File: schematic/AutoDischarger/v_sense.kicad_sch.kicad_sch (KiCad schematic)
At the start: 37 parts, among them IC3 TLV9102SIDGSR, IC4 TLV9102SIDGSR, IC5 TLV9102SIDGSR

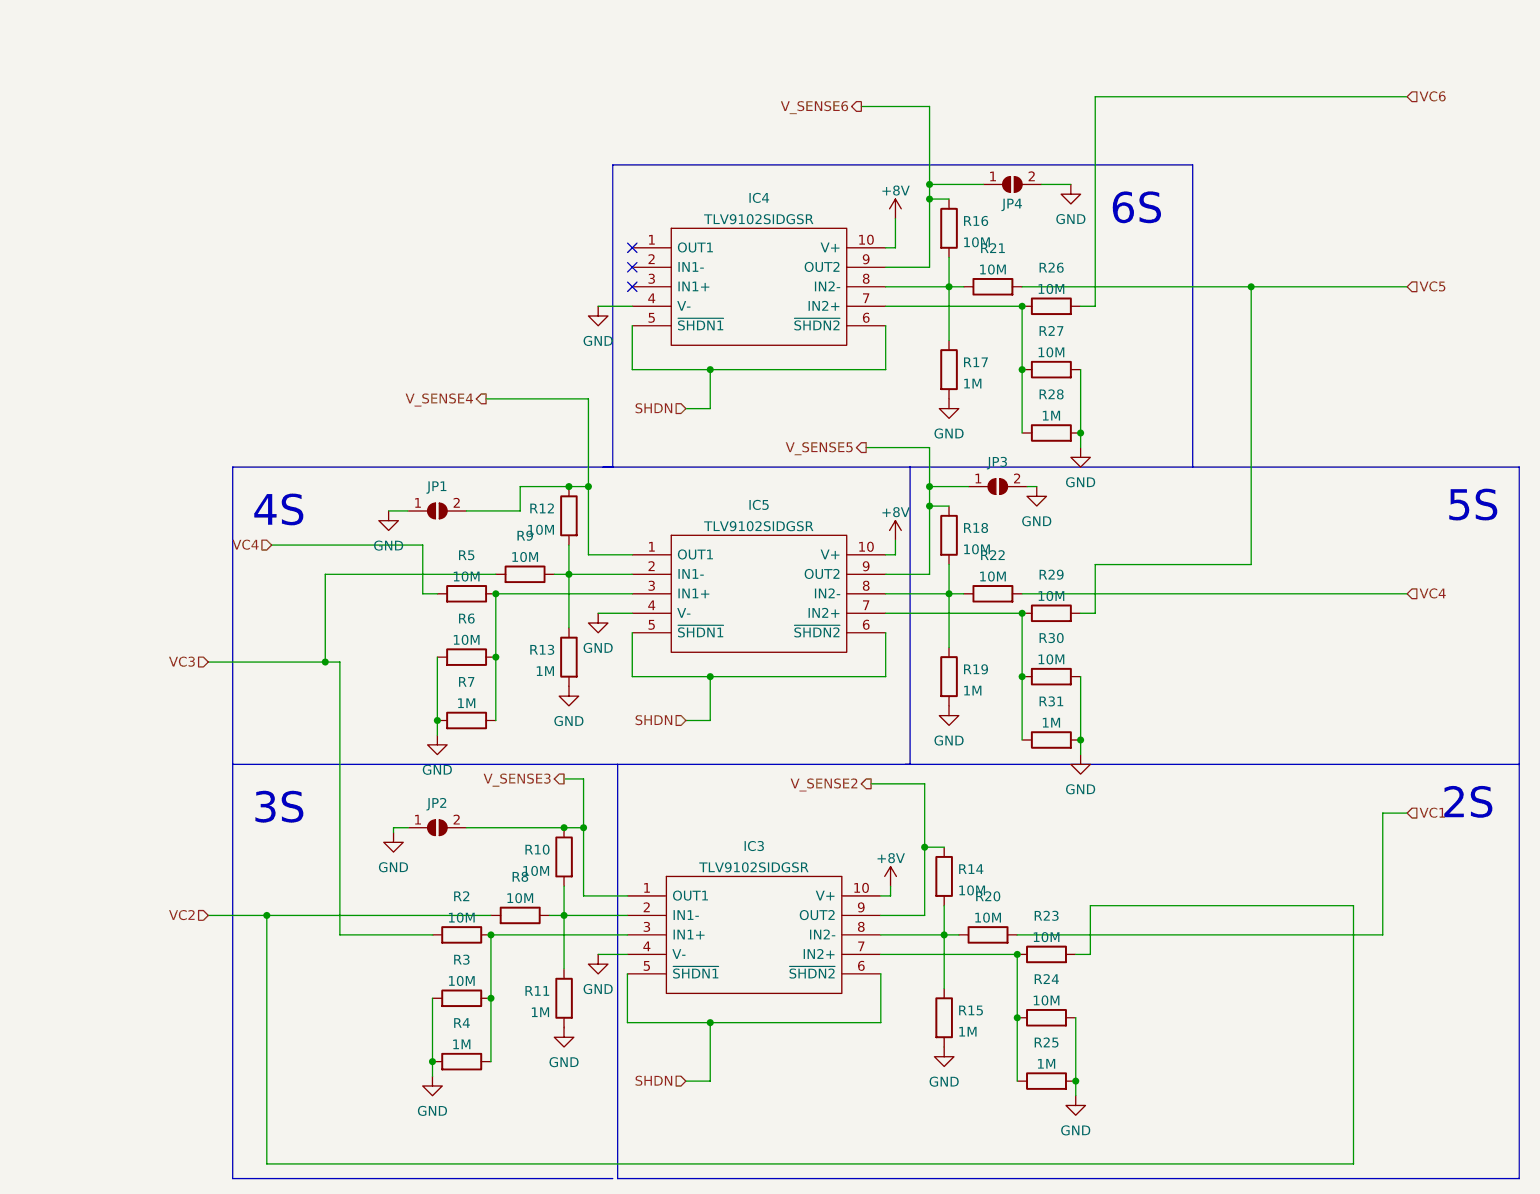
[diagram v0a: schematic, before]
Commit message: Some schematic fixes and assigned footprints.
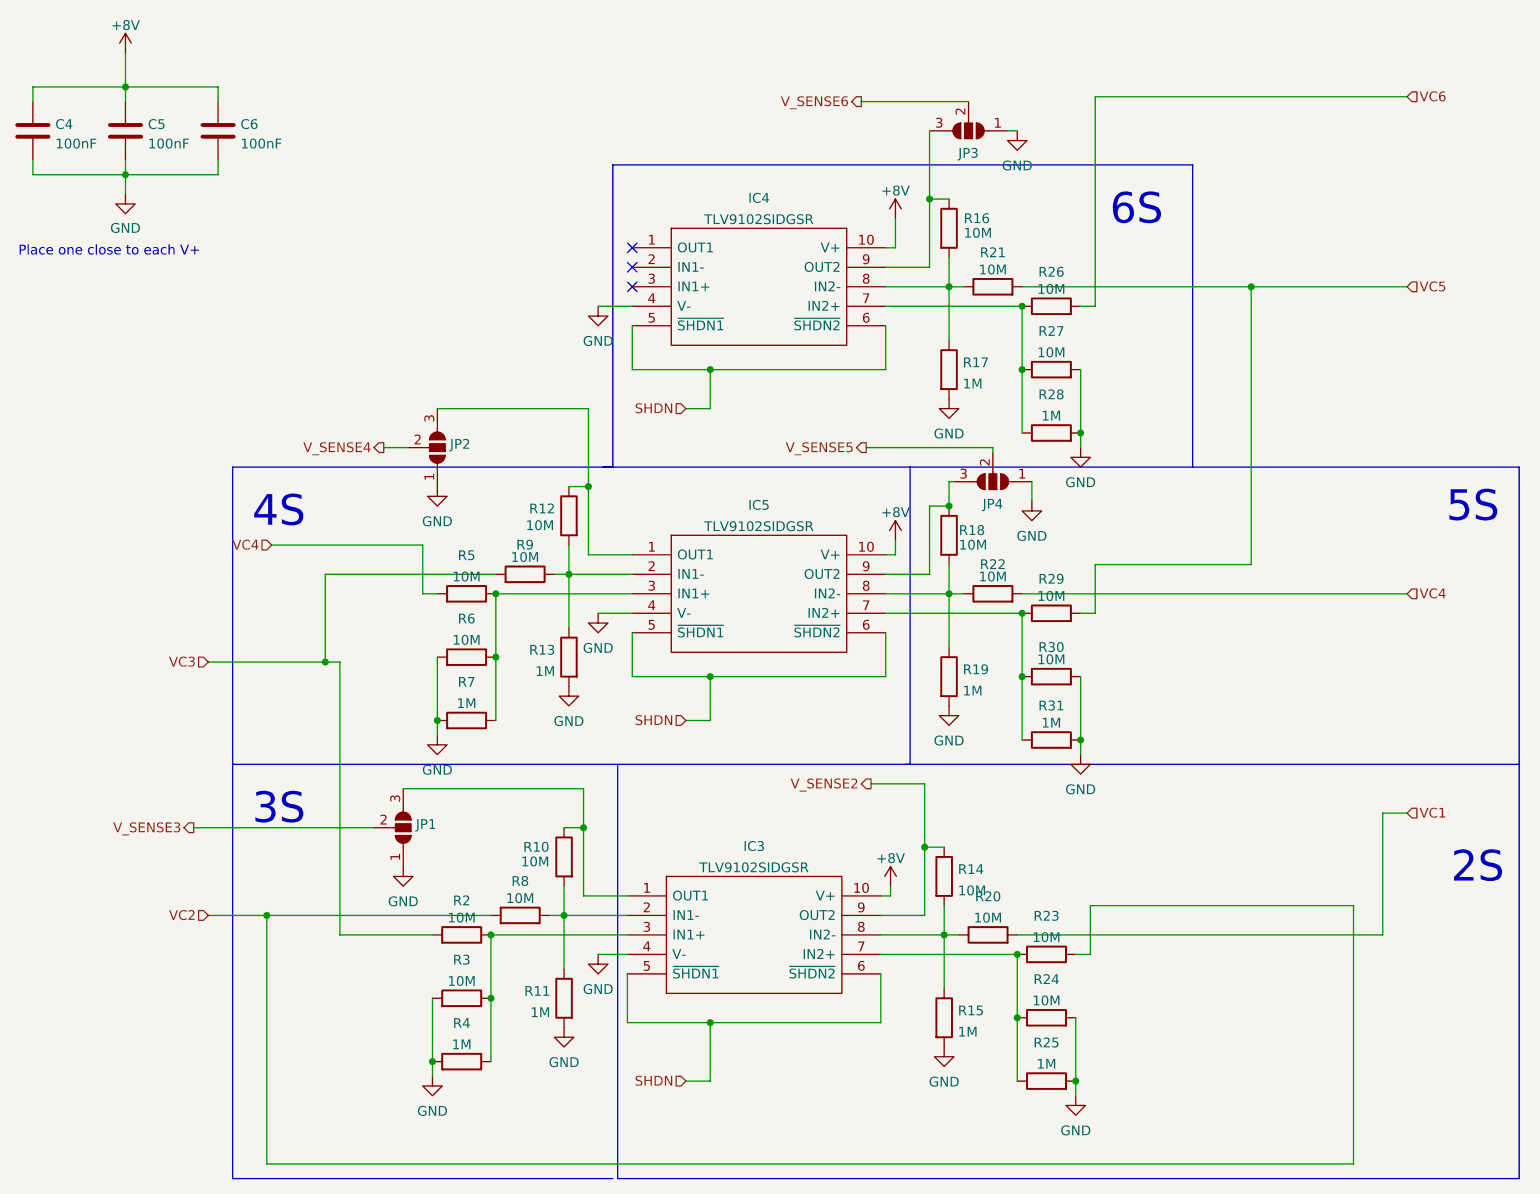
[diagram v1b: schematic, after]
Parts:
- removed JP1, JP2, JP3, JP4: SolderJumper_2_Open, symbol Jumper:SolderJumper_2_Open
- added C4, C5, C6: 100nF, Capacitor_SMD:C_0603_1608Metric, symbol Device:C
- added JP1, JP2, JP3, JP4: SolderJumper_3_Open, Jumper:SolderJumper-3_P1.3mm_Open_RoundedPad1.0x1.5mm_NumberLabels, symbol Jumper:SolderJumper_3_Open
- IC3, IC4, IC5: footprint SOP50P490X110-10N -> SamacSys_Parts:SOP50P490X110-10N
- R10, R11, R12, R13, R14, R15, R16, R17, R18, R19, R2, R20, R21, R22, R23, R24, R25, R26, R27, R28, R29, R3, R30, R31, R4, R5, R6, R7, R8, R9: footprint (none) -> Resistor_SMD:R_0603_1608Metric
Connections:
- net +8V: now also C4.1, C5.1, C6.1
- net GND: now also C4.2, C5.2, C6.2, JP1.1 (A), JP2.1 (A), JP3.1 (A), JP4.1 (A)
- net V_SENSE3: now also JP1.2 (C); no longer IC3.1 (OUT1), R10.1
- net V_SENSE4: now also JP2.2 (C); no longer IC5.1 (OUT1), R12.1
- net V_SENSE5: now also JP4.2 (C); no longer IC5.9 (OUT2), R18.1
- net V_SENSE6: now also JP3.2 (C); no longer IC4.9 (OUT2), R16.1
- new net: IC5.9 (OUT2), JP4.3 (B), R18.1
- new net: IC4.9 (OUT2), JP3.3 (B), R16.1
- new net: IC3.1 (OUT1), JP1.3 (B), R10.1
- new net: IC5.1 (OUT1), JP2.3 (B), R12.1
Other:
- note added: "Place one close to each V+"
- company: Quantum Embedded System -> Quantum Embedded Systems

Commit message: PCB tweaks
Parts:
- renumbered JP4 to JP3, JP3 to JP4
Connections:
- net +8V: now also IC4.5 (~{SHDN1})
- net GND: now also IC4.2 (IN1-), IC4.3 (IN1+)
- net SHDN: no longer IC4.5 (~{SHDN1})
- no-connect marks 3 -> 1
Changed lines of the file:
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@@
   (junction (at 104.775 98.425) (diameter 0) (color 0 0 0 0)
   )
-  (junction (at 132.715 60.96) (diameter 0) (color 0 0 0 0)
-  )
   (junction (at 132.715 100.965) (diameter 0) (color 0 0 0 0)
   )
@@
   (junction (at 173.355 100.965) (diameter 0) (color 0 0 0 0)
   )
+  (junction (at 118.11 52.705) (diameter 0) (color 0 0 0 0)
+  )
   (junction (at 104.775 90.17) (diameter 0) (color 0 0 0 0)
   )
+  (junction (at 118.11 50.165) (diameter 0) (color 0 0 0 0)
+  )
   (junction (at 104.14 142.875) (diameter 0) (color 0 0 0 0)
   )
@@
   )
   (no_connect (at 122.555 45.085))
-  (no_connect (at 122.555 47.625))
-  (no_connect (at 122.555 50.165))
   (wire (pts (xy 68.58 35.56) (xy 68.58 33.655))
     (stroke (width 0) (type default) (color 0 0 0 0))
@@
     (stroke (width 0) (type default) (color 0 0 0 0))
   )
+  (wire (pts (xy 122.555 47.625) (xy 118.11 47.625))
+    (stroke (width 0) (type default) (color 0 0 0 0))
+  )
   (polyline (pts (xy 120.65 112.395) (xy 238.125 112.395))
     (stroke (width 0) (type default) (color 0 0 0 0))
@@
     (stroke (width 0) (type default) (color 0 0 0 0))
   )
+  (wire (pts (xy 118.11 47.625) (xy 118.11 50.165))
+    (stroke (width 0) (type default) (color 0 0 0 0))
+  )
   (wire (pts (xy 104.14 134.62) (xy 104.14 142.875))
     (stroke (width 0) (type default) (color 0 0 0 0))
@@
     (stroke (width 0) (type default) (color 0 0 0 0))
   )
-  (wire (pts (xy 122.555 60.96) (xy 132.715 60.96))
-    (stroke (width 0) (type default) (color 0 0 0 0))
-  )
   (wire (pts (xy 122.555 100.965) (xy 132.715 100.965))
     (stroke (width 0) (type default) (color 0 0 0 0))
@@
     (stroke (width 0) (type default) (color 0 0 0 0))
   )
+  (wire (pts (xy 118.11 50.165) (xy 118.11 52.705))
+    (stroke (width 0) (type default) (color 0 0 0 0))
+  )
   (wire (pts (xy 104.14 142.875) (xy 104.14 151.13))
     (stroke (width 0) (type default) (color 0 0 0 0))
@@
     (stroke (width 0) (type default) (color 0 0 0 0))
   )
-  (wire (pts (xy 122.555 55.245) (xy 122.555 60.96))
-    (stroke (width 0) (type default) (color 0 0 0 0))
-  )
   (wire (pts (xy 121.92 132.08) (xy 113.665 132.08))
     (stroke (width 0) (type default) (color 0 0 0 0))
@@
     (stroke (width 0) (type default) (color 0 0 0 0))
   )
+  (wire (pts (xy 118.11 50.165) (xy 122.555 50.165))
+    (stroke (width 0) (type default) (color 0 0 0 0))
+  )
   (wire (pts (xy 173.355 60.96) (xy 173.355 69.215))
     (stroke (width 0) (type default) (color 0 0 0 0))
@@
   )
   (wire (pts (xy 180.975 60.96) (xy 180.975 69.215))
+    (stroke (width 0) (type default) (color 0 0 0 0))
+  )
+  (wire (pts (xy 122.555 55.245) (xy 122.555 57.785))
     (stroke (width 0) (type default) (color 0 0 0 0))
   )
@@
     (pin "1")
   )
+  (symbol (lib_id "power:+8V") (at 122.555 57.785 180) (unit 1)
+    (in_bom yes) (on_board yes) (fields_autoplaced)
+    (property "Reference" "#PWR?" (id 0) (at 122.555 53.975 0)
+      (effects (font (size 1.27 1.27)) hide)
+    )
+    (property "Value" "+8V" (id 1) (at 122.555 62.2284 0))
+    (property "Footprint" "" (id 2) (at 122.555 57.785 0)
+      (effects (font (size 1.27 1.27)) hide)
+    )
+    (property "Datasheet" "" (id 3) (at 122.555 57.785 0)
+      (effects (font (size 1.27 1.27)) hide)
+    )
+    (pin "1")
+  )
   (symbol (lib_id "power:+8V") (at 156.21 128.27 0) (unit 1)
     (in_bom yes) (on_board yes) (fields_autoplaced)
@@
   (symbol (lib_id "Jumper:SolderJumper_3_Open") (at 166.37 29.845 180) (unit 1)
     (in_bom yes) (on_board yes) (fields_autoplaced)
-    (property "Reference" "JP3" (id 0) (at 166.37 32.7644 0))
+    (property "Reference" "JP4" (id 0) (at 166.37 32.7644 0))
     (property "Value" "SolderJumper_3_Open" (id 1) (at 166.37 31.8969 0)
       (effects (font (size 1.27 1.27)) hide)
@@
   (symbol (lib_id "Jumper:SolderJumper_3_Open") (at 169.545 75.565 180) (unit 1)
     (in_bom yes) (on_board yes) (fields_autoplaced)
-    (property "Reference" "JP4" (id 0) (at 169.545 78.4844 0))
+    (property "Reference" "JP3" (id 0) (at 169.545 78.4844 0))
     (property "Value" "SolderJumper_3_Open" (id 1) (at 169.545 77.6169 0)
       (effects (font (size 1.27 1.27)) hide)
